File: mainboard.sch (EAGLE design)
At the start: 68 parts, among them J1 POWER_JACKPTH_LOCK, T1 SINGLE_NCHAN_FET, T2 MOSFET_PCHAN_20A, T3 SINGLE_NCHAN_FET, T4 MOSFET_PCHAN_20A, T5 SINGLE_NCHAN_FET, T6 MOSFET_PCHAN_20A, T7 MOSFET_PCHAN_20A, T8 SINGLE_NCHAN_FET, U1 MURATA_REG_OKL-T3-W12, U2 TEENSY_3.0+4, U3 RFM23BP, U4 HMC5883LSMD, U5 ITG-3200, U7 CURRENT_MAX4372, U8 CURRENT_MAX4372

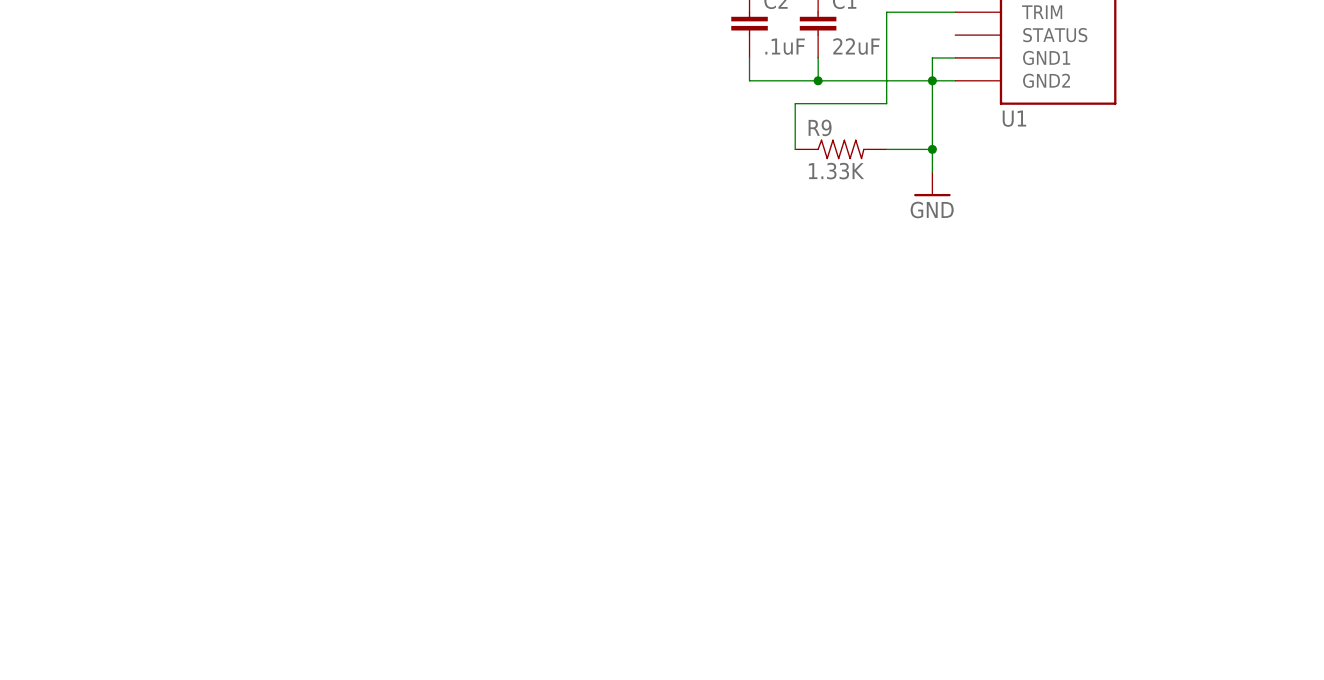
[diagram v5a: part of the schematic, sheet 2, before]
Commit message: added piksi gps connector and enable circuitry. Added molex library
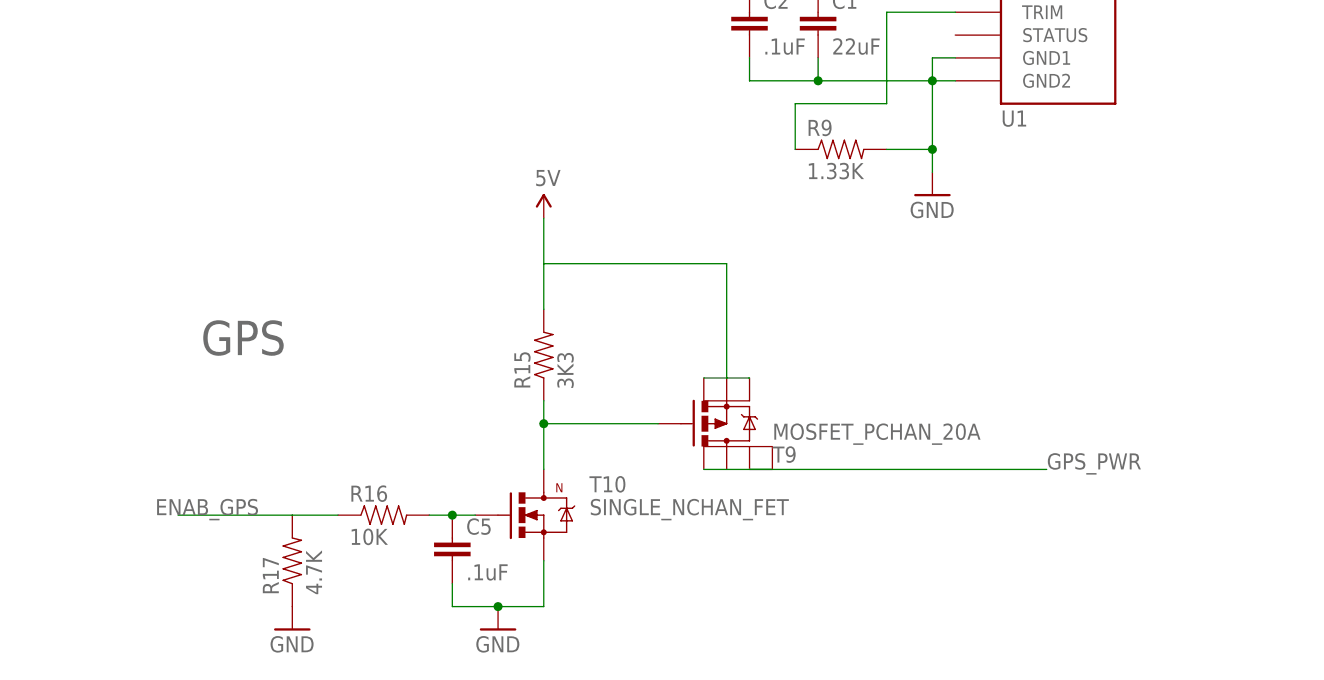
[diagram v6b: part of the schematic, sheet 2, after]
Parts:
- added C5: .1uF, SparkFun-Capacitors:CAP0805
- added R15: 3K3, SparkFun-Resistors:RESISTOR0805-RES
- added R16: 10K, SparkFun-Resistors:RESISTOR0805-RES
- added R17: 4.7K, SparkFun-Resistors:RESISTOR0805-RES
- added T10: SINGLE_NCHAN_FET, phonesat:SINGLE_NCHAN_FET
- added T9: MOSFET_PCHAN_20A, phonesat:MOSFET_PCHAN_20A
- added X1: (no value), pel_molex:CONN_5-1-53398
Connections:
- new net ENAB_GPS: R16.1, R17.2, U2.17/A3
- new net GPS_PWR: T9.D@1, T9.D@2, T9.D@3, T9.D@4, X1.5
- new net N$10: C5.1, R16.2, T10.G
- new net N$12: R15.1, T10.D, T9.G
- net 5V: now also R15.2, T9.S@1, T9.S@2, T9.S@3
- net GND: now also C5.2, R17.1, T10.S, X1.1
- net UART3_RX: now also X1.3
- net UART3_TX: now also X1.2
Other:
- note added: "GPS"
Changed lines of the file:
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@@
 <layer number="223" name="223bmp" color="24" fill="1" visible="no" active="no"/>
 <layer number="224" name="224bmp" color="25" fill="1" visible="no" active="no"/>
+<layer number="231" name="Eagle3D_PG1" color="14" fill="1" visible="yes" active="yes"/>
+<layer number="232" name="Eagle3D_PG2" color="14" fill="2" visible="yes" active="yes"/>
+<layer number="233" name="Eagle3D_PG3" color="14" fill="4" visible="yes" active="yes"/>
 <layer number="248" name="Housing" color="7" fill="1" visible="yes" active="yes"/>
 <layer number="249" name="Edge" color="7" fill="1" visible="yes" active="yes"/>
@@
 <part name="GND19" library="SparkFun" deviceset="GND" device=""/>
 <part name="S3" library="SparkFun-Electromechanical" deviceset="SWITCH-DPDT" device="AYZ0202" value="DPDT"/>
+<part name="GND6" library="SparkFun" deviceset="GND" device=""/>
+<part name="T9" library="phonesat" deviceset="MOSFET_PCHAN_20A" device=""/>
+<part name="T10" library="phonesat" deviceset="SINGLE_NCHAN_FET" device=""/>
+<part name="R15" library="SparkFun-Resistors" deviceset="RESISTOR" device="0805-RES" value="3K3"/>
+<part name="C5" library="SparkFun-Capacitors" deviceset="CAP" device="0805" value=".1uF"/>
+<part name="R16" library="SparkFun-Resistors" deviceset="RESISTOR" device="0805-RES" value="10K"/>
+<part name="R17" library="SparkFun-Resistors" deviceset="RESISTOR" device="0805-RES" value="4.7K"/>
+<part name="GND22" library="SparkFun" deviceset="GND" device=""/>
+<part name="U$1" library="SparkFun" deviceset="5V" device=""/>
+<part name="X1" library="pel_molex" deviceset="CONN_5-1" device="-53398"/>
+<part name="GND23" library="SparkFun-Aesthetics" deviceset="GND" device=""/>
 </parts>
 <sheets>
@@
 </segment>
 </net>
+<net name="ENAB_GPS" class="0">
+<segment>
+<pinref part="U2" gate="G$1" pin="17/A3"/>
+<wire x1="81.28" y1="-25.4" x2="121.92" y2="-25.4" width="0.1524" layer="91"/>
+<label x="111.76" y="-25.4" size="1.778" layer="95"/>
+</segment>
+</net>
 </nets>
 </sheet>
@@
 <text x="-76.2" y="-10.16" size="1.778" layer="97">Battery Current Sensor</text>
 <text x="71.12" y="-119.38" size="3.81" layer="95">BW4</text>
+<text x="-86.36" y="-119.38" size="3.81" layer="95">GPS</text>
 </plain>
 <instances>
@@
 <instance part="R13" gate="G$1" x="81.28" y="-142.24" rot="R90"/>
 <instance part="GND4" gate="1" x="81.28" y="-149.86"/>
+<instance part="GND6" gate="1" x="-53.34" y="-149.86"/>
+<instance part="T9" gate="G$1" x="-27.94" y="-127"/>
+<instance part="T10" gate="G$1" x="-50.8" y="-137.16"/>
+<instance part="R15" gate="G$1" x="-48.26" y="-119.38" rot="R90"/>
+<instance part="C5" gate="G$1" x="-58.42" y="-142.24"/>
+<instance part="R16" gate="G$1" x="-66.04" y="-137.16"/>
+<instance part="R17" gate="G$1" x="-76.2" y="-142.24" rot="R90"/>
+<instance part="GND22" gate="1" x="-76.2" y="-149.86"/>
+<instance part="U$1" gate="G$1" x="-48.26" y="-104.14"/>
 </instances>
 <busses>
@@
 <pinref part="GND4" gate="1" pin="GND"/>
 </segment>
+<segment>
+<wire x1="-48.26" y1="-142.24" x2="-48.26" y2="-147.32" width="0.1524" layer="91"/>
+<pinref part="T10" gate="G$1" pin="S"/>
+<pinref part="C5" gate="G$1" pin="2"/>
+<wire x1="-58.42" y1="-144.78" x2="-58.42" y2="-147.32" width="0.1524" layer="91"/>
+<wire x1="-58.42" y1="-147.32" x2="-53.34" y2="-147.32" width="0.1524" layer="91"/>
+<pinref part="GND6" gate="1" pin="GND"/>
+<wire x1="-53.34" y1="-147.32" x2="-48.26" y2="-147.32" width="0.1524" layer="91"/>
+<junction x="-53.34" y="-147.32"/>
+</segment>
+<segment>
+<pinref part="R17" gate="G$1" pin="1"/>
+<pinref part="GND22" gate="1" pin="GND"/>
+</segment>
 </net>
 <net name="VBURN1" class="0">
@@
 <pinref part="U$2" gate="G$1" pin="5V"/>
 </segment>
+<segment>
+<pinref part="T9" gate="G$1" pin="S@3"/>
+<pinref part="T9" gate="G$1" pin="S@1"/>
+<wire x1="-25.4" y1="-121.92" x2="-27.94" y2="-121.92" width="0.1524" layer="91"/>
+<pinref part="T9" gate="G$1" pin="S@2"/>
+<wire x1="-27.94" y1="-121.92" x2="-30.48" y2="-121.92" width="0.1524" layer="91"/>
+<wire x1="-27.94" y1="-121.92" x2="-27.94" y2="-109.22" width="0.1524" layer="91"/>
+<wire x1="-27.94" y1="-109.22" x2="-48.26" y2="-109.22" width="0.1524" layer="91"/>
+<pinref part="R15" gate="G$1" pin="2"/>
+<wire x1="-48.26" y1="-109.22" x2="-48.26" y2="-114.3" width="0.1524" layer="91"/>
+<wire x1="-48.26" y1="-109.22" x2="-48.26" y2="-104.14" width="0.1524" layer="91"/>
+<pinref part="U$1" gate="G$1" pin="5V"/>
+</segment>
 </net>
 <net name="N$8" class="0">
@@
 <wire x1="-2.54" y1="-71.12" x2="-45.72" y2="-71.12" width="0.1524" layer="91"/>
 <label x="-45.72" y="-71.12" size="1.778" layer="95"/>
+</segment>
+</net>
+<net name="N$10" class="0">
+<segment>
+<wire x1="-60.96" y1="-137.16" x2="-58.42" y2="-137.16" width="0.1524" layer="91"/>
+<wire x1="-58.42" y1="-137.16" x2="-55.88" y2="-137.16" width="0.1524" layer="91"/>
+<junction x="-58.42" y="-137.16"/>
+<pinref part="R16" gate="G$1" pin="2"/>
+<pinref part="C5" gate="G$1" pin="1"/>
+<pinref part="T10" gate="G$1" pin="G"/>
+</segment>
+</net>
+<net name="N$12" class="0">
+<segment>
+<pinref part="T10" gate="G$1" pin="D"/>
+<pinref part="T9" gate="G$1" pin="G"/>
+<wire x1="-35.56" y1="-127" x2="-48.26" y2="-127" width="0.1524" layer="91"/>
+<wire x1="-48.26" y1="-127" x2="-48.26" y2="-132.08" width="0.1524" layer="91"/>
+<pinref part="R15" gate="G$1" pin="1"/>
+<wire x1="-48.26" y1="-127" x2="-48.26" y2="-124.46" width="0.1524" layer="91"/>
+<junction x="-48.26" y="-127"/>
+</segment>
+</net>
+<net name="ENAB_GPS" class="0">
+<segment>
+<pinref part="R16" gate="G$1" pin="1"/>
+<pinref part="R17" gate="G$1" pin="2"/>
+<wire x1="-71.12" y1="-137.16" x2="-76.2" y2="-137.16" width="0.1524" layer="91"/>
+<wire x1="-76.2" y1="-137.16" x2="-88.9" y2="-137.16" width="0.1524" layer="91"/>
+<label x="-91.44" y="-137.16" size="1.778" layer="95"/>
+</segment>
+</net>
+<net name="GPS_PWR" class="0">
+<segment>
+<pinref part="T9" gate="G$1" pin="D@2"/>
+<pinref part="T9" gate="G$1" pin="D@3"/>
+<wire x1="-30.48" y1="-132.08" x2="-27.94" y2="-132.08" width="0.1524" layer="91"/>
+<pinref part="T9" gate="G$1" pin="D@4"/>
+<wire x1="-22.86" y1="-132.08" x2="-25.4" y2="-132.08" width="0.1524" layer="91"/>
+<pinref part="T9" gate="G$1" pin="D@1"/>
+<wire x1="-25.4" y1="-132.08" x2="-27.94" y2="-132.08" width="0.1524" layer="91"/>
+<wire x1="-25.4" y1="-132.08" x2="7.62" y2="-132.08" width="0.1524" layer="91"/>
+<label x="7.62" y="-132.08" size="1.778" layer="95"/>
 </segment>
 </net>
@@
 <instance part="ST5" gate="G$1" x="-17.78" y="60.96" rot="R180"/>
 <instance part="J1" gate="G$1" x="15.24" y="109.22" rot="MR0"/>
+<instance part="X1" gate="G$1" x="-25.4" y="20.32"/>
+<instance part="GND23" gate="1" x="-38.1" y="10.16"/>
 </instances>
 <busses>
@@
 <pinref part="GND5" gate="1" pin="GND"/>
 <wire x1="-25.4" y1="58.42" x2="-25.4" y2="55.88" width="0.1524" layer="91"/>
+</segment>
+<segment>
+<pinref part="X1" gate="G$1" pin="1"/>
+<wire x1="-30.48" y1="15.24" x2="-38.1" y2="15.24" width="0.1524" layer="91"/>
+<wire x1="-38.1" y1="15.24" x2="-38.1" y2="12.7" width="0.1524" layer="91"/>
+<pinref part="GND23" gate="1" pin="GND"/>
 </segment>
 </net>
@@
 </segment>
 </net>
+<net name="GPS_PWR" class="0">
+<segment>
+<pinref part="X1" gate="G$1" pin="5"/>
+<wire x1="-30.48" y1="25.4" x2="-38.1" y2="25.4" width="0.1524" layer="91"/>
+<label x="-50.8" y="25.4" size="1.778" layer="95"/>
+</segment>
+</net>
+<net name="UART3_TX" class="0">
+<segment>
+<pinref part="X1" gate="G$1" pin="2"/>
+<wire x1="-30.48" y1="17.78" x2="-38.1" y2="17.78" width="0.1524" layer="91"/>
+<label x="-50.8" y="17.78" size="1.778" layer="95"/>
+</segment>
+</net>
+<net name="UART3_RX" class="0">
+<segment>
+<pinref part="X1" gate="G$1" pin="3"/>
+<wire x1="-30.48" y1="20.32" x2="-38.1" y2="20.32" width="0.1524" layer="91"/>
+<label x="-50.8" y="20.32" size="1.778" layer="95"/>
+</segment>
+</net>

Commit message: Schematic clean-up
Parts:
- added FRAME1, FRAME2, FRAME3: FRAME-LETTER, SparkFun-Aesthetics:FRAME-LETTER
- X1: device pel_molex:CONN_5-1-53398 -> pel_molex:CONN_5-1-53261
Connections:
- net N$11: now also S3.1; no longer S3.3
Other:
- note added: "3"
- note added: "Burn Wire 1"
- note added: "Burn Wire 2"
- note added: "Burn Wire 3"
- note added: "Burn Wire 4"
- note added: "Current Limiting Resistors for Burn Wires"
- note added: "GPS Power"
- note added: "Piksi GPS Connector"
- note added: "Zac Manchester"
- note removed: "BW1"
- note removed: "BW2"
- note removed: "BW3"
- note removed: "BW4"
- note removed: "Burn Wires"
- note removed: "GPS"
- moved on the sheet: C1, C12, C13, C14, C15, C16, C17, C18, C19, C2, C20, C3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

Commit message: Mainboard routing work
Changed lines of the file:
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@@
 <text x="17.78" y="33.02" size="2.54" layer="95">Burn Wire 4</text>
 <text x="104.14" y="149.86" size="1.778" layer="97">Current Limiting Resistors for Burn Wires</text>
-<text x="170.18" y="7.62" size="3.175" layer="94">Zac Manchester</text>
+<text x="172.72" y="7.62" size="3.175" layer="94">Zac Manchester</text>
 <text x="241.3" y="7.62" size="2.54" layer="94">3</text>
 <text x="144.78" y="63.5" size="2.54" layer="95">GPS Power</text>
